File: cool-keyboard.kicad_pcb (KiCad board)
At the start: 2 copper layers, 81.9 x 87.4 mm, 22 parts, among them SW1 SW_Push_45deg, SW10 SW_Push_45deg, SW2 SW_Push_45deg, SW3 SW_Push_45deg, SW4 SW_Push_45deg, SW5 SW_Push_45deg, SW6 SW_Push_45deg, SW7 SW_Push_45deg, SW8 SW_Push_45deg, SW9 SW_Push_45deg, U2 MOUDLE-SEEEDUINO-XIAO

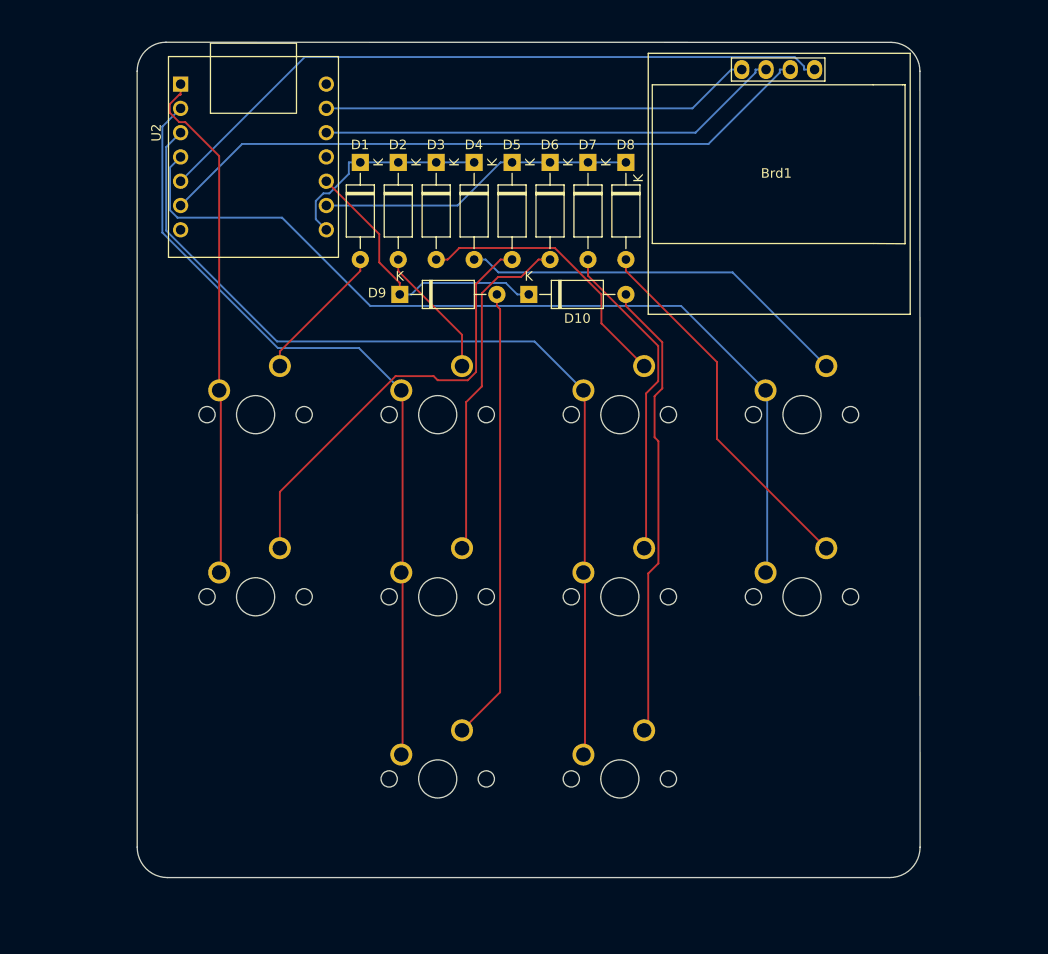
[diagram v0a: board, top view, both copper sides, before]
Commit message: add ground fill
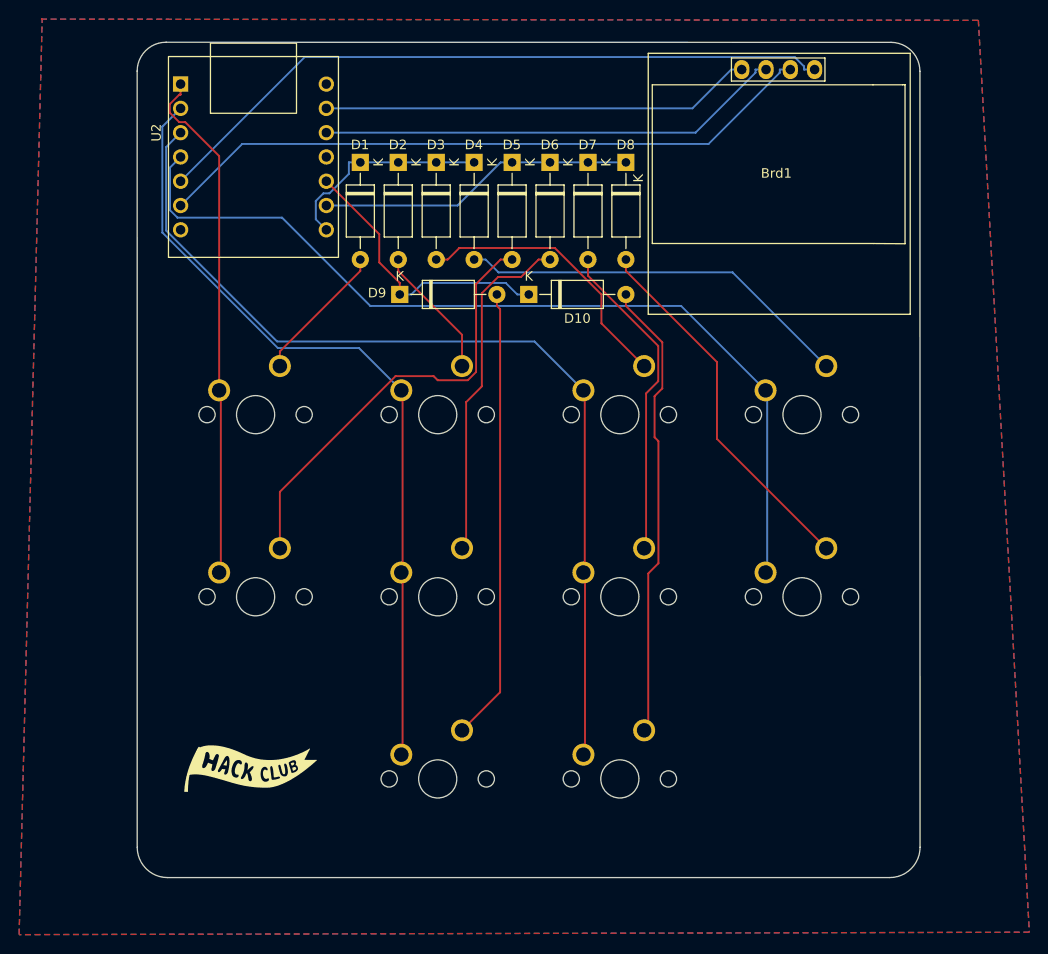
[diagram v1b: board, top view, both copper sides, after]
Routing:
- added copper zone on B.Cu, net GND
- added copper zone on F.Cu, net GND
